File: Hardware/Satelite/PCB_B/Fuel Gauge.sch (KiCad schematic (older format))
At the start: 5 parts

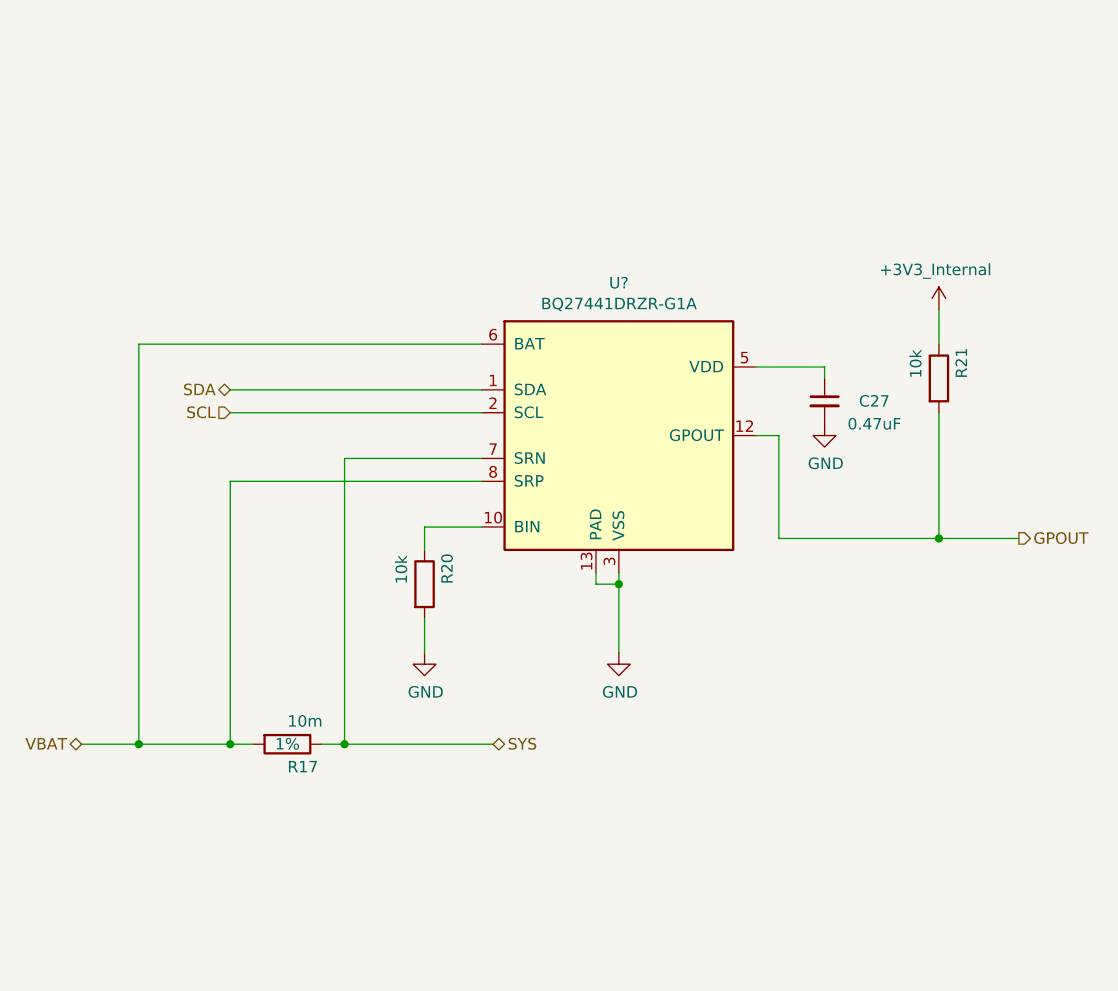
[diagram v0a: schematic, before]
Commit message: Arreglos en PCB_A y PCB_B:
- El CI cargador de batería ya no alimenta al sistema, al conectar un cargador el mismo alimenta a la batería y al sistema de manera simultánea
- Ya no es necesario encender el CanSat para cargar la batería
- El interruptor del PCB_A ahora apaga todo el sistema independientemente si se está cargando o no la batería
- Agregado LED indicador de carga de batería
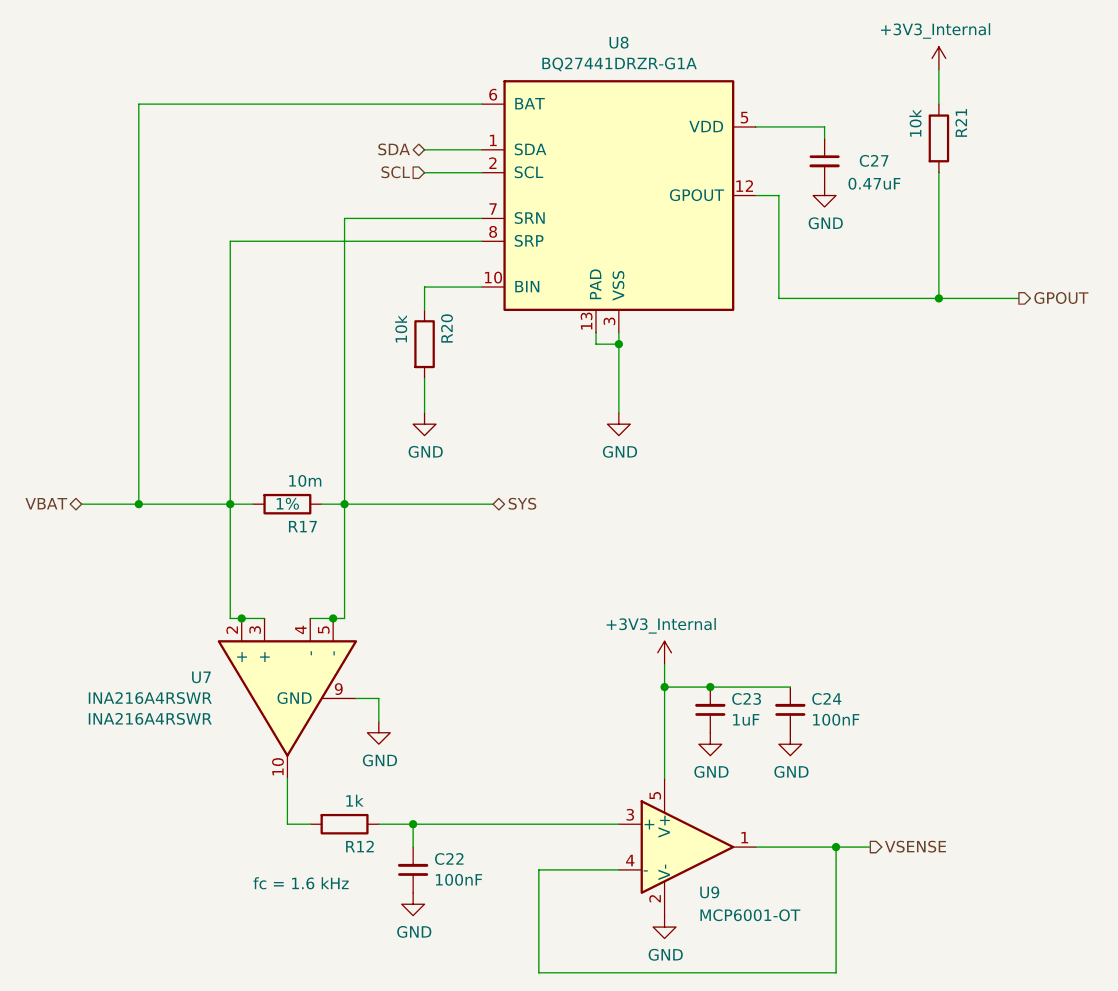
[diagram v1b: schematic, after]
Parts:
- added C22, C24: 100nF, Capacitor_SMD:C_0603_1608Metric_Pad1.05x0.95mm_HandSolder, symbol Device:C_Small
- added C23: 1uF, Capacitor_SMD:C_0603_1608Metric_Pad1.05x0.95mm_HandSolder, symbol Device:C_Small
- added R12: 1k, Capacitor_SMD:C_0603_1608Metric_Pad1.05x0.95mm_HandSolder, symbol Device:R
- added U7: INA216A4RSWR, Package_DFN_QFN:UQFN-10_1.4x1.8mm_P0.4mm, symbol AXTEC_IC:INA216A4RSWR
- added U9: MCP6001-OT, Package_TO_SOT_SMD:SOT-23-5, symbol Amplifier_Operational:MCP6001-OT
- gave numbers to parts that had none: 1
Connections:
- net +3V3_Internal: now also C23.2, C24.2, U9.5 (V+)
- net GND: now also C22.1, C23.1, C24.1, U7.9 (GND), U9.2 (V-)
- net SYS: now also U7.4 (-), U7.5 (-)
- net VBAT: now also U7.2 (+), U7.3 (+)
- new net: C22.2, R12.1, U9.3 (+)
- new net: R12.2, U7.10
- new net VSENSE: U9.1, U9.4 (-)
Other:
- note added: "fc = 1.6 kHz"
- moved on the sheet: C27, R17, R20, R21, U8

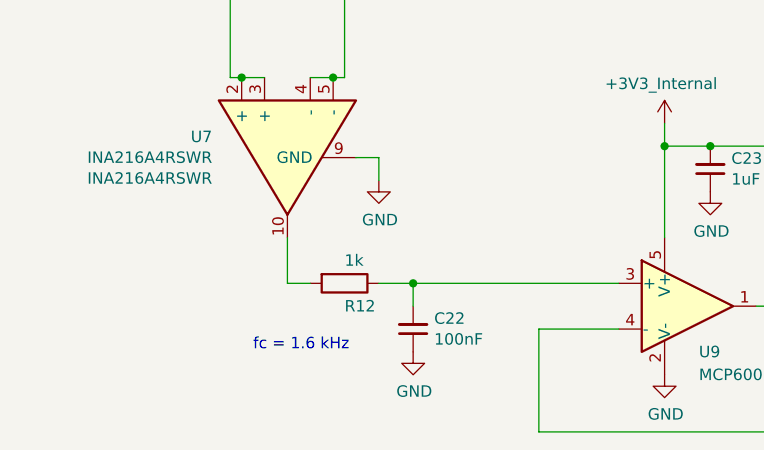
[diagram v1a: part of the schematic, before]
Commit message: Agregado de MOSFET para cortar las fuentes de 3.3V y 5V en el PCB_B en lugar de usar los enable
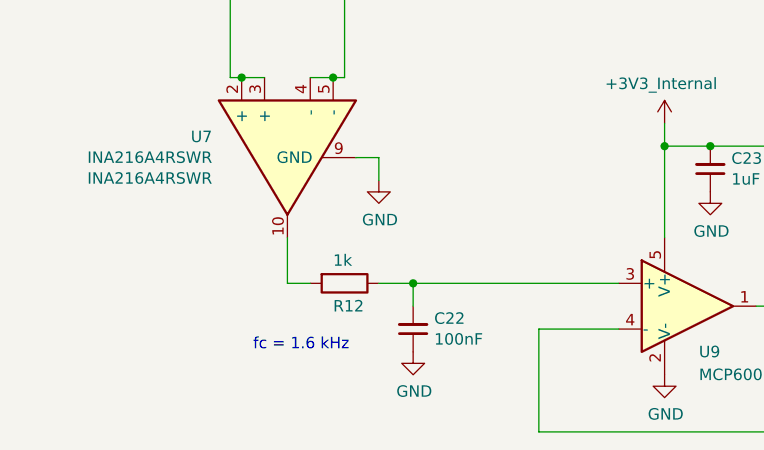
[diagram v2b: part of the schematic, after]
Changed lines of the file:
@@
 AR Path="/5BB1631B/5CEAECF7" Ref="R?"  Part="1"
 AR Path="/5BC28DAC/5CEAECF7" Ref="R12"  Part="1"
-F 0 "R12" V 4800 5400 50  0000 L CNN
-F 1 "1k" V 4600 5400 50  0000 L CNN
+F 0 "R12" V 4800 5350 50  0000 L CNN
+F 1 "1k" V 4600 5350 50  0000 L CNN
 F 2 "Capacitor_SMD:C_0603_1608Metric_Pad1.05x0.95mm_HandSolder" V 4630 5400 50  0001 C CNN
 F 3 "~" H 4700 5400 50  0001 C CNN

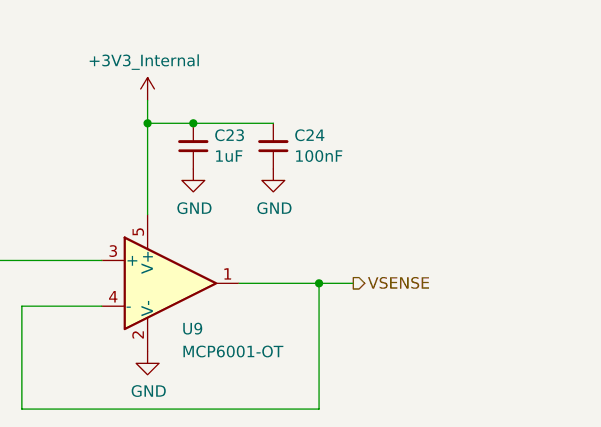
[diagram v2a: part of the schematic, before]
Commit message: Fixed wrong label in fuel gauge schematic
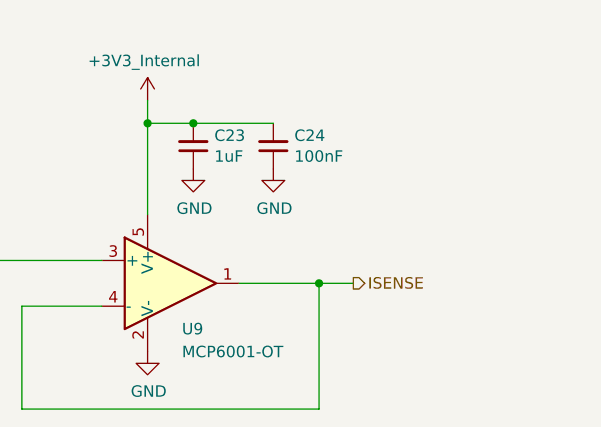
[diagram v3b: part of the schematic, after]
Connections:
- net VSENSE renamed ISENSE
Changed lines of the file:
@@
 $EndBitmap
 Text HLabel 7000 5500 2    50   Output ~ 0
-VSENSE
+ISENSE
 $Comp
 L Amplifier_Operational:MCP6001-OT U?

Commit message: PCB_B V2 terminado
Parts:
- U7: footprint Package_DFN_QFN:UQFN-10_1.4x1.8mm_P0.4mm -> Package_DFN_QFN:UQFN-10_1.3x1.8mm_P0.4mm
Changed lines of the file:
@@
 F 0 "U7" V 4259 4779 50  0000 L CNN
 F 1 "INA216A4RSWR" V 4350 4779 50  0000 L CNN
-F 2 "Package_DFN_QFN:UQFN-10_1.4x1.8mm_P0.4mm" H 4200 4950 50  0001 C CNN
+F 2 "Package_DFN_QFN:UQFN-10_1.3x1.8mm_P0.4mm" H 4200 4950 50  0001 C CNN
 F 3 "" H 4200 4950 50  0001 C CNN
 F 4 "INA216A4RSWR" V 4441 4779 50  0000 L CNN "Manufacturer Part Number"
